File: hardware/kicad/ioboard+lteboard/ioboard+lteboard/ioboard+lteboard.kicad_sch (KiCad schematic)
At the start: 0 parts

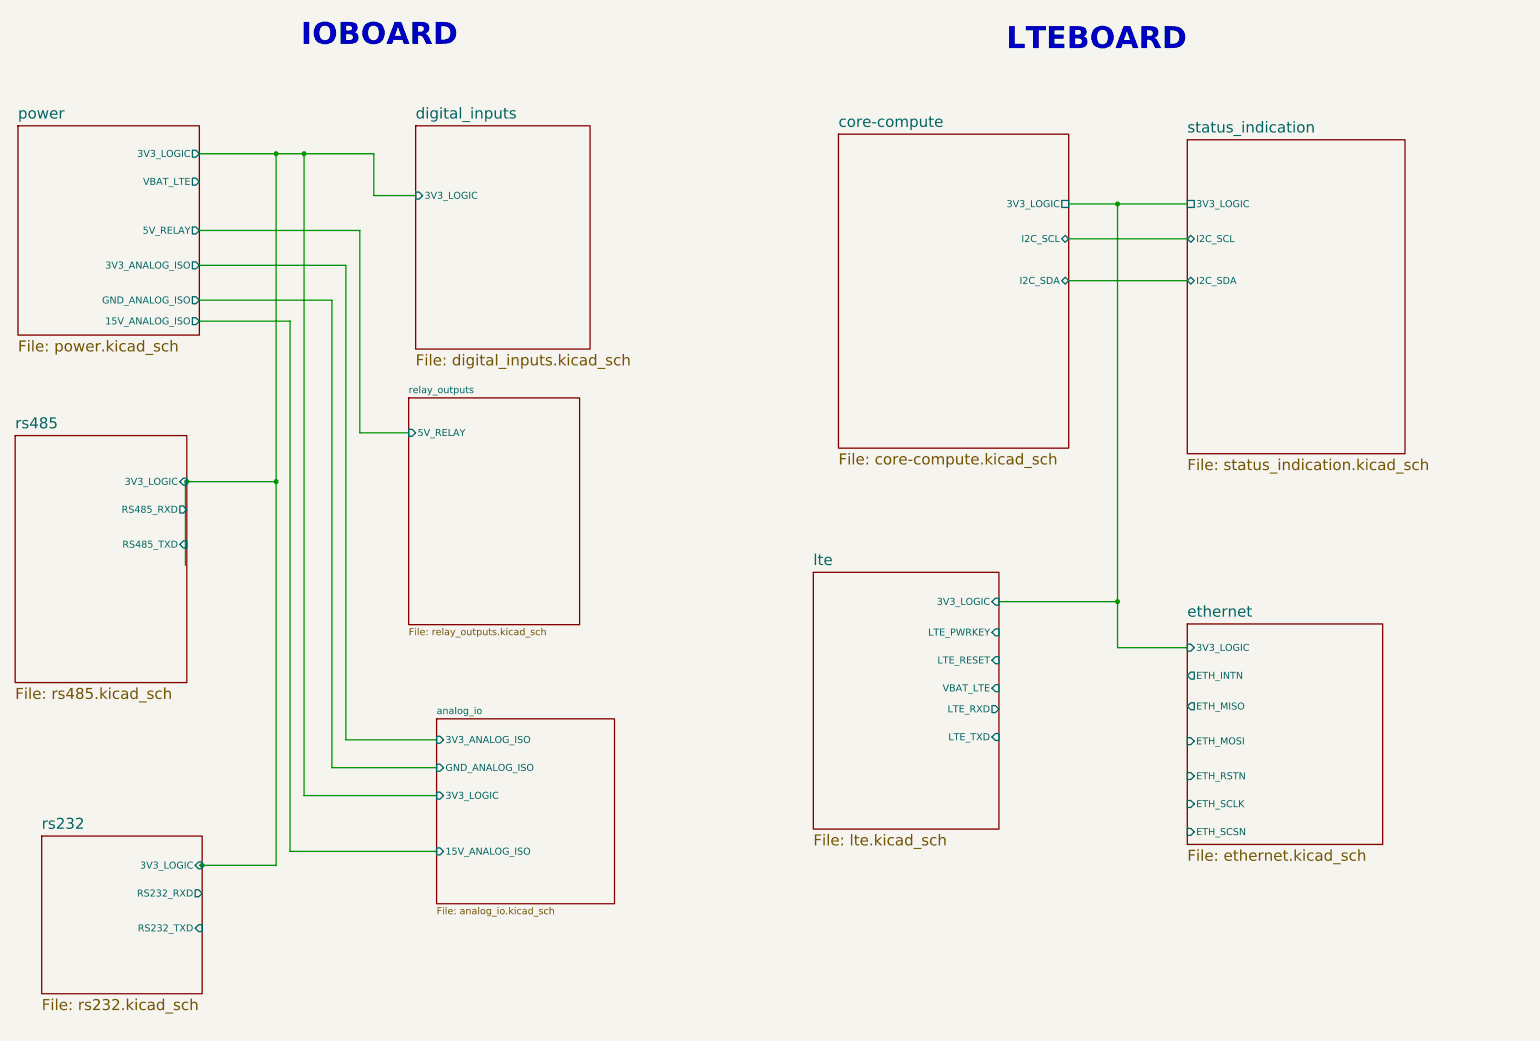
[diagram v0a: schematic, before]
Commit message: Step 6: pin assignment and wiring on ioboard+lteboard
- core-compute: fix USB D+/D- to native GPIO19/GPIO20 (was on GPIO13/14)
- analog_io: expose ISO1540 logic-side I2C as hierarchical labels (bidirectional)
- core-compute: add 14 hierarchical labels for ethernet/lte/rs485/rs232 pin assignment
- root sheet: wire all 14 signals to their subsystems, confirm I2C 3-way merge
  (analog_io + core-compute + status_indication)
- root sheet: VBAT_LTE tied power<->lte (casual, ahead of the formal
  board-to-board connector decision, which stays a step 7 item; 3V3_LOGIC
  intentionally left split for the same reason)
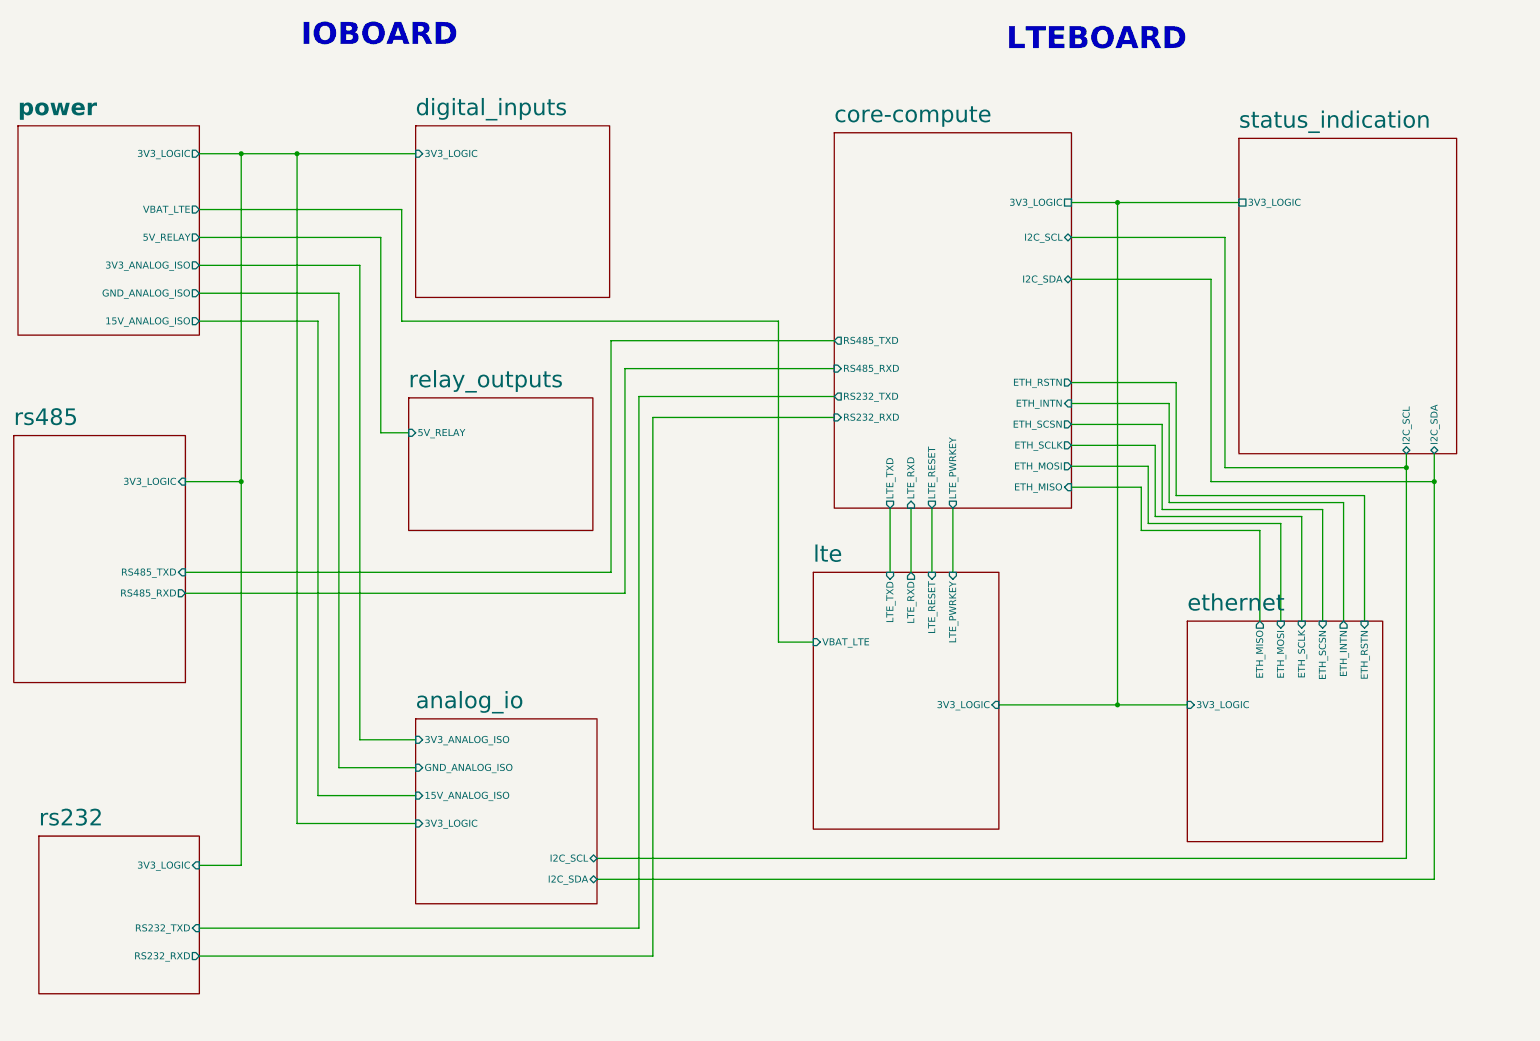
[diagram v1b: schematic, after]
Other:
- sheet analog_io ports: added I2C_SCL, I2C_SDA; removed none
- sheet core-compute ports: added ETH_INTN, ETH_MISO, ETH_MOSI, ETH_RSTN, ETH_SCLK, ETH_SCSN, LTE_PWRKEY, LTE_RESET, LTE_RXD, LTE_TXD, RS232_RXD, RS232_TXD, RS485_RXD, RS485_TXD; removed none

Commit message: added missing hierarchical labels for core-compute, digitil_inputs and relay_output
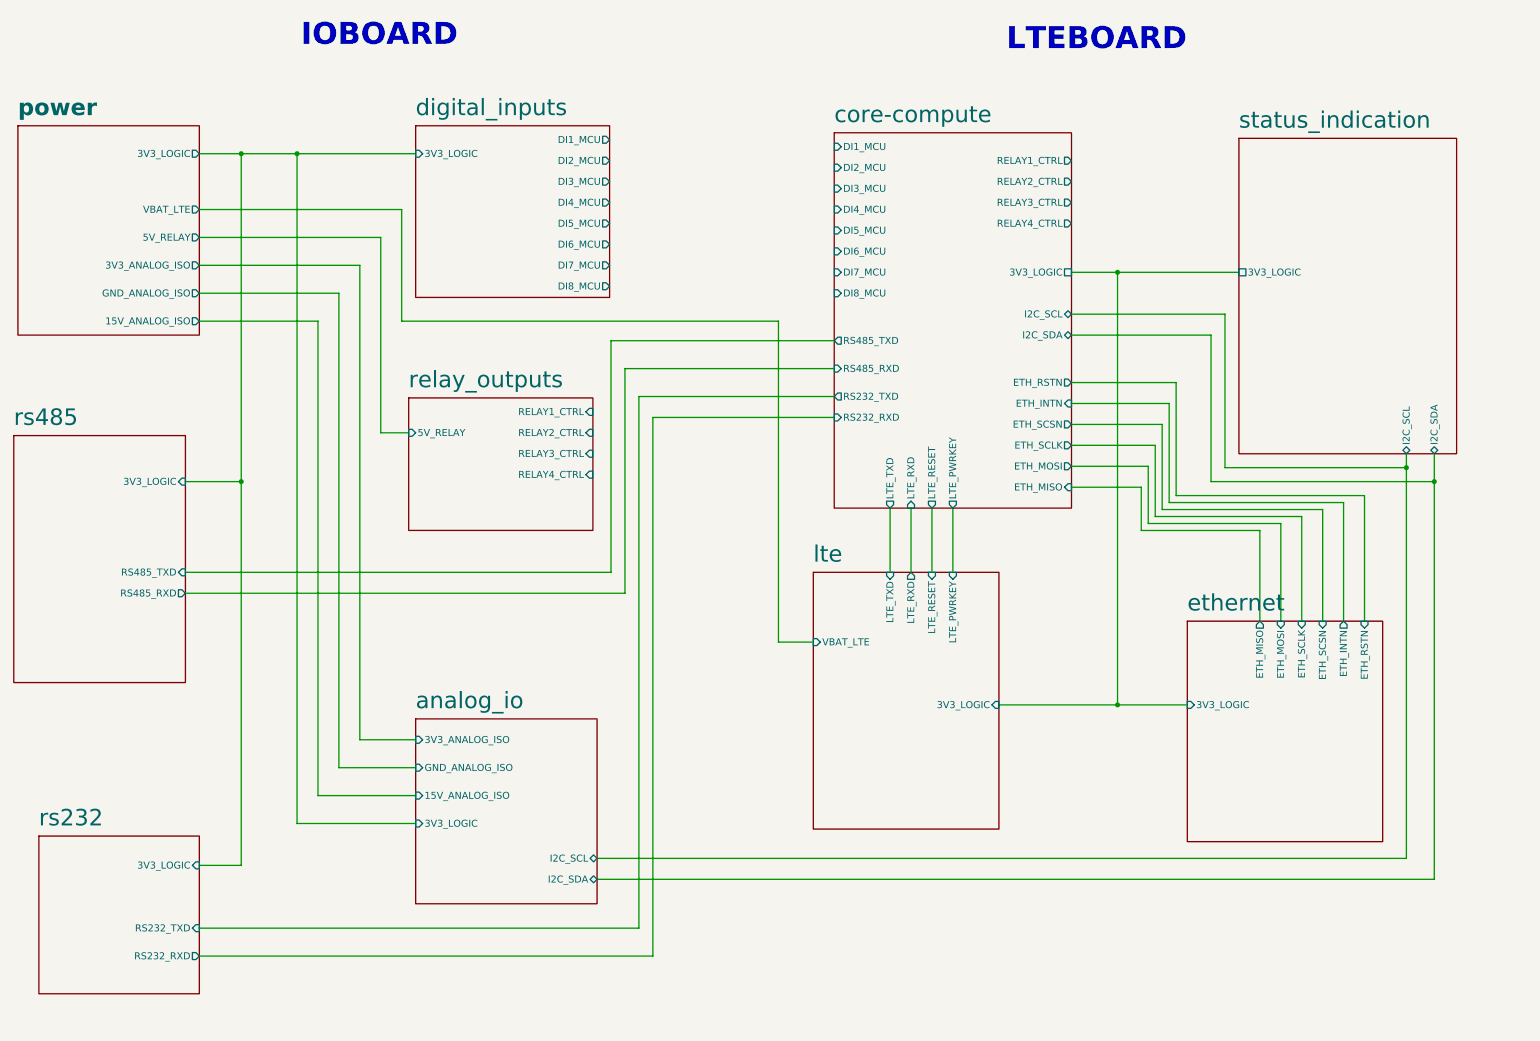
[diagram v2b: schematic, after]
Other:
- sheet core-compute ports: added DI1_MCU, DI2_MCU, DI3_MCU, DI4_MCU, DI5_MCU, DI6_MCU, DI7_MCU, DI8_MCU, RELAY1_CTRL, RELAY2_CTRL, RELAY3_CTRL, RELAY4_CTRL; removed none
- sheet digital_inputs ports: added DI1_MCU, DI2_MCU, DI3_MCU, DI4_MCU, DI5_MCU, DI6_MCU, DI7_MCU, DI8_MCU; removed none
- sheet relay_outputs ports: added RELAY1_CTRL, RELAY2_CTRL, RELAY3_CTRL, RELAY4_CTRL; removed none
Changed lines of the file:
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@@
-	)
-	(junction
-		(at 219.202 35.56)
-		(diameter 0)
-		(color 0 0 0 0)
 	)
 	(junction
@@
 		(color 0 0 0 0)
 	)
+	(junction
+		(at 219.202 48.26)
+		(diameter 0)
+		(color 0 0 0 0)
+	)
 	(wire
 		(pts
@@
 	(wire
 		(pts
-			(xy 210.82 49.53) (xy 236.22 49.53)
-		)
-		(stroke
-			(width 0)
-			(type default)
-		)
-	)
-	(wire
-		(pts
-			(xy 236.22 49.53) (xy 236.22 86.36)
+			(xy 210.82 59.69) (xy 236.22 59.69)
+		)
+		(stroke
+			(width 0)
+			(type default)
+		)
+	)
+	(wire
+		(pts
+			(xy 236.22 59.69) (xy 236.22 86.36)
 		)
 		(stroke
@@
 	(wire
 		(pts
-			(xy 219.202 35.56) (xy 241.3 35.56)
+			(xy 219.202 48.26) (xy 241.3 48.26)
 		)
 		(stroke
@@
 	(wire
 		(pts
-			(xy 238.76 41.91) (xy 238.76 83.82)
+			(xy 238.76 55.88) (xy 238.76 83.82)
 		)
 		(stroke
@@
 	(wire
 		(pts
-			(xy 210.82 35.56) (xy 219.202 35.56)
+			(xy 210.82 48.26) (xy 219.202 48.26)
 		)
 		(stroke
@@
 	(wire
 		(pts
+			(xy 219.202 48.26) (xy 219.202 127)
+		)
+		(stroke
+			(width 0)
+			(type default)
+		)
+	)
+	(wire
+		(pts
 			(xy 69.85 26.67) (xy 91.44 26.67)
 		)
@@
 	(wire
 		(pts
-			(xy 219.202 35.56) (xy 219.202 127)
-		)
-		(stroke
-			(width 0)
-			(type default)
-		)
-	)
-	(wire
-		(pts
-			(xy 210.82 41.91) (xy 238.76 41.91)
+			(xy 210.82 55.88) (xy 238.76 55.88)
 		)
 		(stroke
@@
 		)
 		(pin "3V3_LOGIC" passive
-			(at 210.82 35.56 0)
+			(at 210.82 48.26 0)
 			(effects
 				(font
@@
 		)
 		(pin "I2C_SCL" bidirectional
-			(at 210.82 41.91 0)
+			(at 210.82 55.88 0)
 			(effects
 				(font
@@
 		)
 		(pin "I2C_SDA" bidirectional
-			(at 210.82 49.53 0)
+			(at 210.82 59.69 0)
 			(effects
 				(font
@@
 		(pin "RS485_TXD" output
 			(at 167.64 60.706 180)
+			(effects
+				(font
+					(size 1.27 1.27)
+				)
+				(justify left)
+			)
+		)
+		(pin "DI2_MCU" input
+			(at 167.64 29.21 180)
+			(effects
+				(font
+					(size 1.27 1.27)
+				)
+				(justify left)
+			)
+		)
+		(pin "DI4_MCU" input
+			(at 167.64 36.83 180)
+			(effects
+				(font
+					(size 1.27 1.27)
+				)
+				(justify left)
+			)
+		)
+		(pin "DI1_MCU" input
+			(at 167.64 25.4 180)
+			(effects
+				(font
+					(size 1.27 1.27)
+				)
+				(justify left)
+			)
+		)
+		(pin "RELAY2_CTRL" output
+			(at 210.82 31.75 0)
+			(effects
+				(font
+					(size 1.27 1.27)
+				)
+				(justify right)
+			)
+		)
+		(pin "RELAY1_CTRL" output
+			(at 210.82 27.94 0)
+			(effects
+				(font
+					(size 1.27 1.27)
+				)
+				(justify right)
+			)
+		)
+		(pin "RELAY3_CTRL" output
+			(at 210.82 35.56 0)
+			(effects
+				(font
+					(size 1.27 1.27)
+				)
+				(justify right)
+			)
+		)
+		(pin "DI6_MCU" input
+			(at 167.64 44.45 180)
+			(effects
+				(font
+					(size 1.27 1.27)
+				)
+				(justify left)
+			)
+		)
+		(pin "DI8_MCU" input
+			(at 167.64 52.07 180)
+			(effects
+				(font
+					(size 1.27 1.27)
+				)
+				(justify left)
+			)
+		)
+		(pin "DI7_MCU" input
+			(at 167.64 48.26 180)
+			(effects
+				(font
+					(size 1.27 1.27)
+				)
+				(justify left)
+			)
+		)
+		(pin "RELAY4_CTRL" output
+			(at 210.82 39.37 0)
+			(effects
+				(font
+					(size 1.27 1.27)
+				)
+				(justify right)
+			)
+		)
+		(pin "DI3_MCU" input
+			(at 167.64 33.02 180)
+			(effects
+				(font
+					(size 1.27 1.27)
+				)
+				(justify left)
+			)
+		)
+		(pin "DI5_MCU" input
+			(at 167.64 40.64 180)
 			(effects
 				(font
@@
 		)
 		(pin "3V3_LOGIC" passive
-			(at 241.3 35.56 180)
+			(at 241.3 48.26 180)
 			(effects
 				(font
@@
 			)
 		)
+		(pin "RELAY2_CTRL" input
+			(at 123.698 77.47 0)
+			(effects
+				(font
+					(size 1.27 1.27)
+				)
+				(justify right)
+			)
+		)
+		(pin "RELAY1_CTRL" input
+			(at 123.698 73.66 0)
+			(effects
+				(font
+					(size 1.27 1.27)
+				)
+				(justify right)
+			)
+		)
+		(pin "RELAY4_CTRL" input
+			(at 123.698 85.09 0)
+			(effects
+				(font
+					(size 1.27 1.27)
+				)
+				(justify right)
+			)
+		)
+		(pin "RELAY3_CTRL" input
+			(at 123.698 81.28 0)
+			(effects
+				(font
+					(size 1.27 1.27)
+				)
+				(justify right)
+			)
+		)
 		(instances
 			(project "ioboard+lteboard"
@@
 			)
 		)
+		(pin "DI5_MCU" output
+			(at 126.746 39.37 0)
+			(effects
+				(font
+					(size 1.27 1.27)
+				)
+				(justify right)
+			)
+		)
+		(pin "DI3_MCU" output
+			(at 126.746 31.75 0)
+			(effects
+				(font
+					(size 1.27 1.27)
+				)
+				(justify right)
+			)
+		)
+		(pin "DI1_MCU" output
+			(at 126.746 24.13 0)
+			(effects
+				(font
+					(size 1.27 1.27)
+				)
+				(justify right)
+			)
+		)
+		(pin "DI4_MCU" output
+			(at 126.746 35.56 0)
+			(effects
+				(font
+					(size 1.27 1.27)
+				)
+				(justify right)
+			)
+		)
+		(pin "DI2_MCU" output
+			(at 126.746 27.94 0)
+			(effects
+				(font
+					(size 1.27 1.27)
+				)
+				(justify right)
+			)
+		)
+		(pin "DI7_MCU" output
+			(at 126.746 46.99 0)
+			(effects
+				(font
+					(size 1.27 1.27)
+				)
+				(justify right)
+			)
+		)
+		(pin "DI6_MCU" output
+			(at 126.746 43.18 0)
+			(effects
+				(font
+					(size 1.27 1.27)
+				)
+				(justify right)
+			)
+		)
+		(pin "DI8_MCU" output
+			(at 126.746 50.8 0)
+			(effects
+				(font
+					(size 1.27 1.27)
+				)
+				(justify right)
+			)
+		)

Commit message: Close roadmap steps 6/7: pin assignment, board-to-board wiring, ERC pass clean; update docs to match
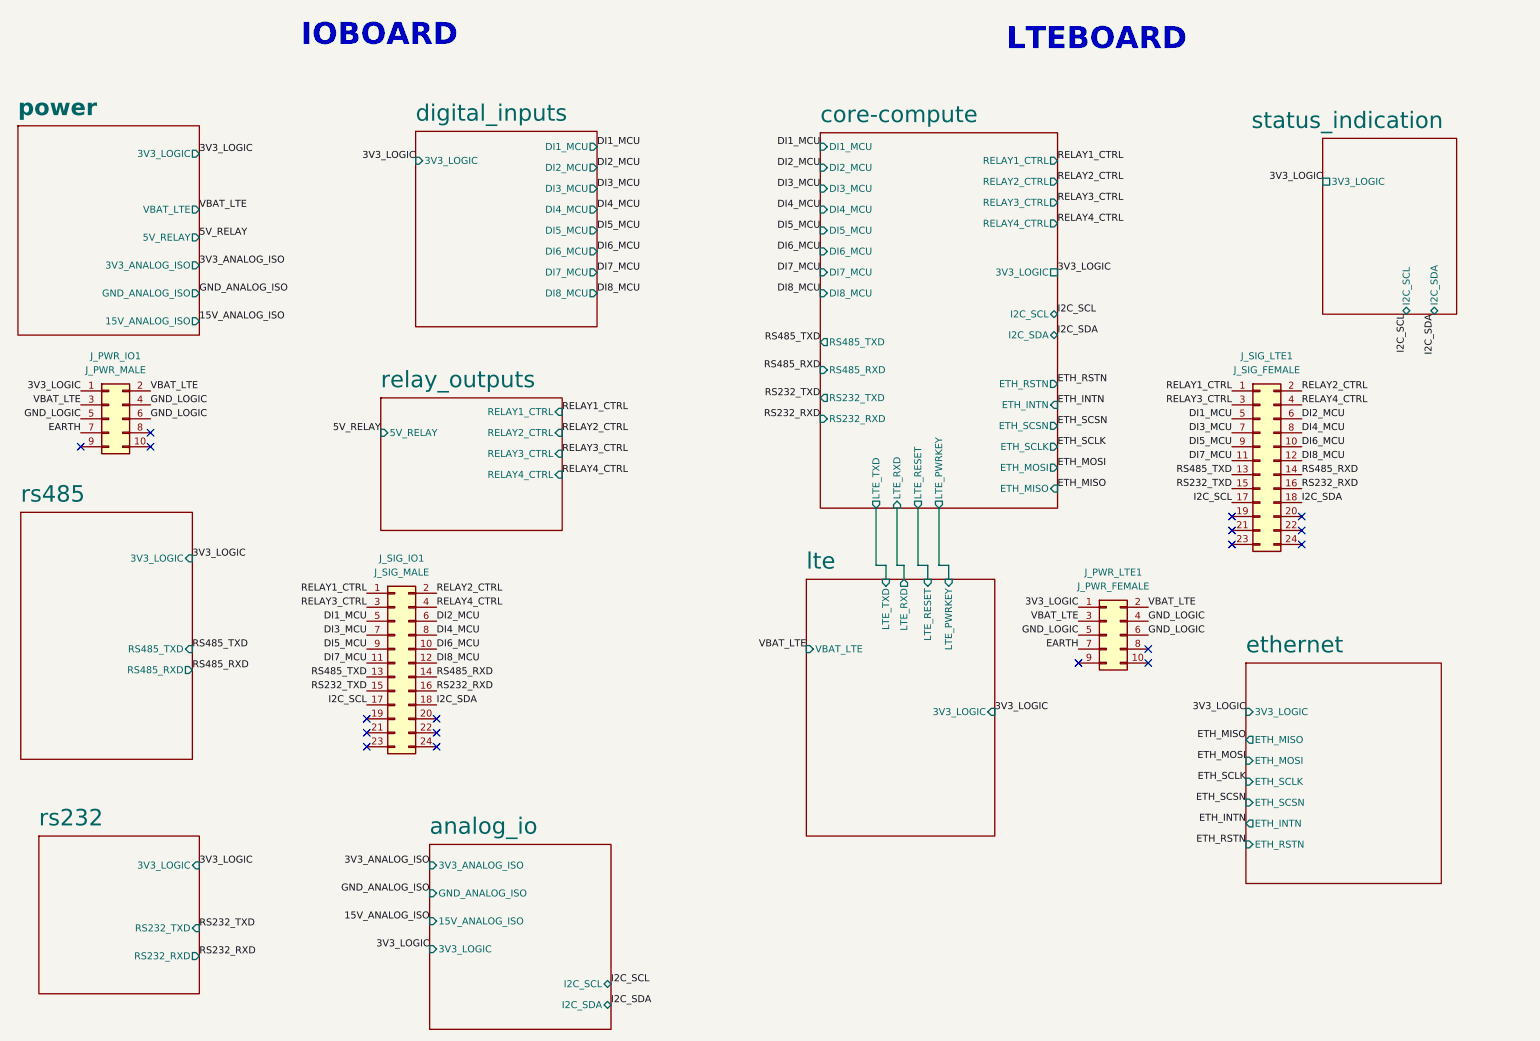
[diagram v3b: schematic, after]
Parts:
- added J_PWR_IO1: J_PWR_MALE, symbol Connector_Generic:Conn_02x05_Odd_Even
- added J_PWR_LTE1: J_PWR_FEMALE, symbol Connector_Generic:Conn_02x05_Odd_Even
- added J_SIG_IO1: J_SIG_MALE, symbol Connector_Generic:Conn_02x12_Odd_Even
- added J_SIG_LTE1: J_SIG_FEMALE, symbol Connector_Generic:Conn_02x12_Odd_Even
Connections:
- new net 3V3_LOGIC: J_PWR_IO1.1 (Pin_1), J_PWR_LTE1.1 (Pin_1)
- new net DI1_MCU: J_SIG_IO1.5 (Pin_5), J_SIG_LTE1.5 (Pin_5)
- new net DI2_MCU: J_SIG_IO1.6 (Pin_6), J_SIG_LTE1.6 (Pin_6)
- new net DI3_MCU: J_SIG_IO1.7 (Pin_7), J_SIG_LTE1.7 (Pin_7)
- new net DI4_MCU: J_SIG_IO1.8 (Pin_8), J_SIG_LTE1.8 (Pin_8)
- new net DI5_MCU: J_SIG_IO1.9 (Pin_9), J_SIG_LTE1.9 (Pin_9)
- new net DI6_MCU: J_SIG_IO1.10 (Pin_10), J_SIG_LTE1.10 (Pin_10)
- new net DI7_MCU: J_SIG_IO1.11 (Pin_11), J_SIG_LTE1.11 (Pin_11)
- new net DI8_MCU: J_SIG_IO1.12 (Pin_12), J_SIG_LTE1.12 (Pin_12)
- new net EARTH: J_PWR_IO1.7 (Pin_7), J_PWR_LTE1.7 (Pin_7)
- new net GND_LOGIC: J_PWR_IO1.4 (Pin_4), J_PWR_IO1.5 (Pin_5), J_PWR_IO1.6 (Pin_6), J_PWR_LTE1.4 (Pin_4), J_PWR_LTE1.5 (Pin_5), J_PWR_LTE1.6 (Pin_6)
- new net I2C_SCL: J_SIG_IO1.17 (Pin_17), J_SIG_LTE1.17 (Pin_17)
- new net I2C_SDA: J_SIG_IO1.18 (Pin_18), J_SIG_LTE1.18 (Pin_18)
- new net RELAY1_CTRL: J_SIG_IO1.1 (Pin_1), J_SIG_LTE1.1 (Pin_1)
- new net RELAY2_CTRL: J_SIG_IO1.2 (Pin_2), J_SIG_LTE1.2 (Pin_2)
- new net RELAY3_CTRL: J_SIG_IO1.3 (Pin_3), J_SIG_LTE1.3 (Pin_3)
- new net RELAY4_CTRL: J_SIG_IO1.4 (Pin_4), J_SIG_LTE1.4 (Pin_4)
- new net RS232_RXD: J_SIG_IO1.16 (Pin_16), J_SIG_LTE1.16 (Pin_16)
- new net RS232_TXD: J_SIG_IO1.15 (Pin_15), J_SIG_LTE1.15 (Pin_15)
- new net RS485_RXD: J_SIG_IO1.14 (Pin_14), J_SIG_LTE1.14 (Pin_14)
- new net RS485_TXD: J_SIG_IO1.13 (Pin_13), J_SIG_LTE1.13 (Pin_13)
- new net VBAT_LTE: J_PWR_IO1.2 (Pin_2), J_PWR_IO1.3 (Pin_3), J_PWR_LTE1.2 (Pin_2), J_PWR_LTE1.3 (Pin_3)
- no-connect marks 0 -> 18
